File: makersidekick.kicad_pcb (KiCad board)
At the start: 2 copper layers, 58.9 x 22.9 mm, 11 parts, among them J2 Conn_01x12, J4 Conn_01x16

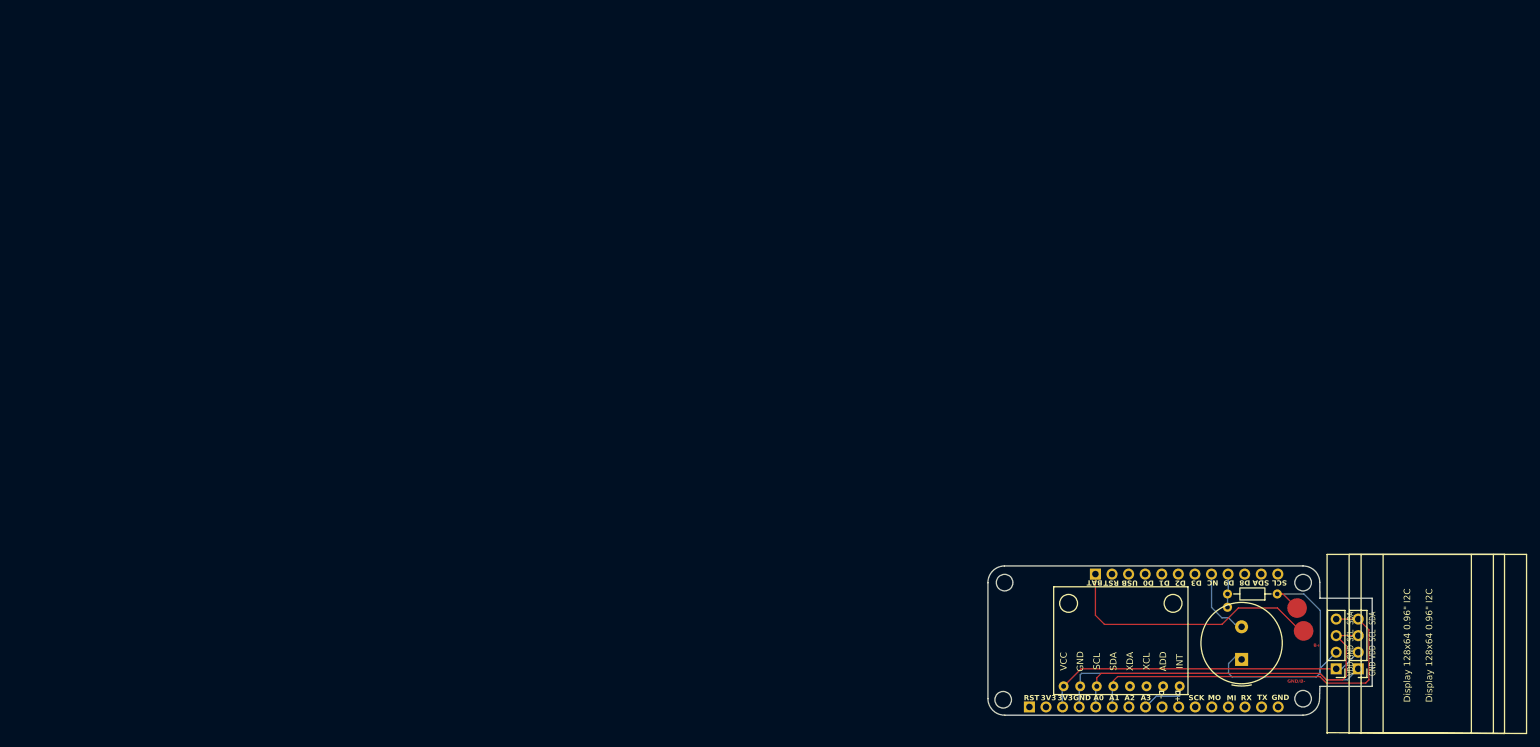
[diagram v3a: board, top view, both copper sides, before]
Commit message: Add buttons, shift text and reroute a lot
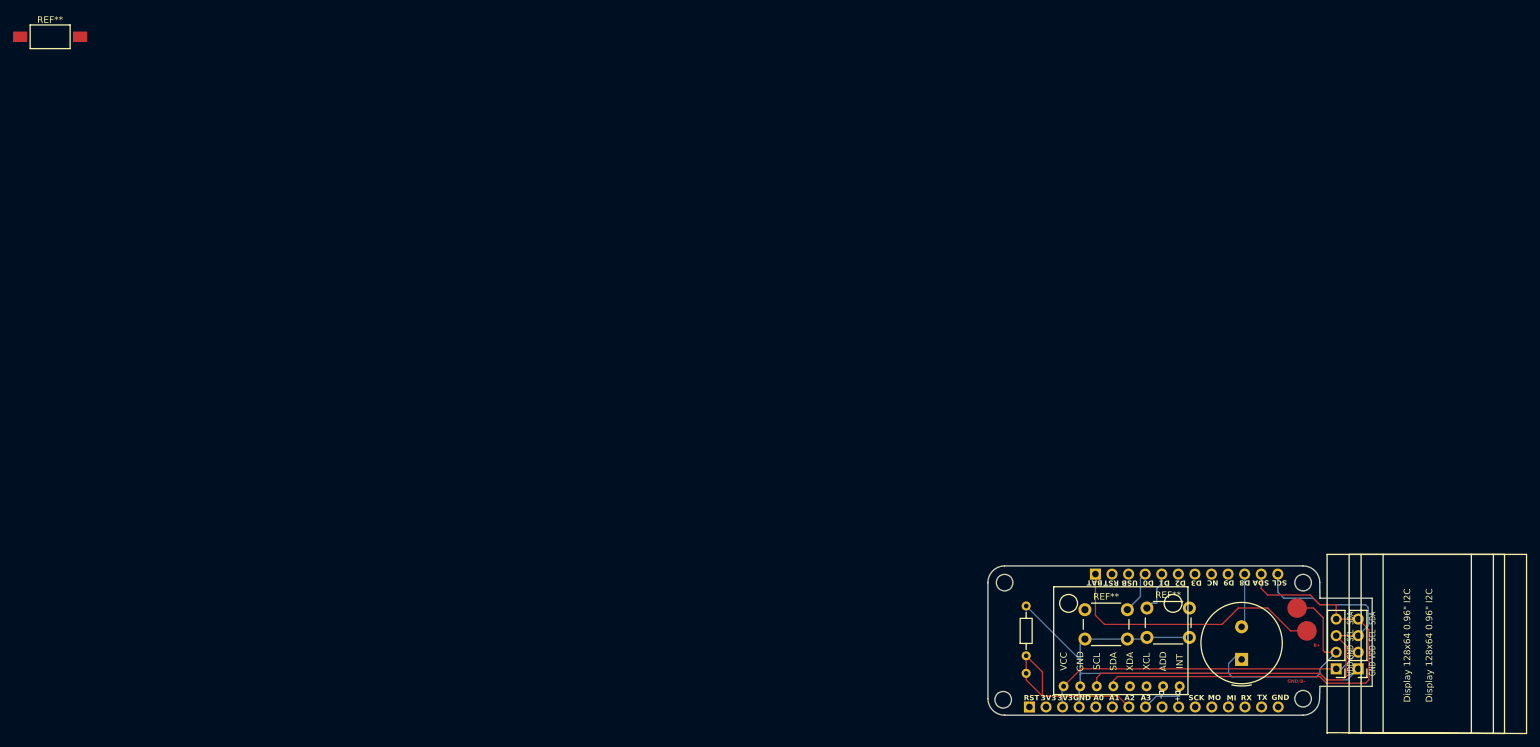
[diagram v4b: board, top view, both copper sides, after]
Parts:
- added REF**: SW_SPST_FSMSM, Button_Switch_SMD:SW_SPST_FSMSM, F.Cu at (0.00, 0.00)
- added REF**: SW_PUSH_6mm_H5mm, Button_Switch_THT:SW_PUSH_6mm_H5mm, F.Cu at (158.5, 87.8)
- added REF**: SW_PUSH_6mm_H5mm, Button_Switch_THT:SW_PUSH_6mm_H5mm, F.Cu at (168.0, 87.5)
- moved REF** 39.6 mm to (149.5, 94.8), turned to 90 degrees
- moved ? 32.5 mm to (149.5, 97.5)
- moved ? 0.50 mm to (192.5, 91.0)
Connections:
- ? pad 2: D9 -> A2
- Display 128x64 0.96" I2C pad 1: (no net) -> gnd
- Display 128x64 0.96" I2C pad 2: (no net) -> 3v3
- Display 128x64 0.96" I2C pad 3: (no net) -> SCL (x2)
- Display 128x64 0.96" I2C pad 4: (no net) -> SDA (x2)
- Display 128x64 0.96" I2C pad 1: (no net) -> 3v3
- Display 128x64 0.96" I2C pad 2: (no net) -> gnd
- J2 pad 10: unconnected-(J2-Pin_10-Pad10) -> D8
- J2 pad 11: unconnected-(J2-Pin_11-Pad11) -> SDA
- J2 pad 12: unconnected-(J2-Pin_12-Pad12) -> SCL
- J2 pad 4: unconnected-(J2-Pin_4-Pad4) -> D0
- J2 pad 5: unconnected-(J2-Pin_5-Pad5) -> D1
- J2 pad 8: D8 -> NC
- J4 pad 7: unconnected-(J4-Pin_7-Pad7) -> A2
- REF** pad 1: gnd -> A2
- REF** pad 2: D9 -> gnd
- REF** pad 3: A0 -> SCL
- REF** pad 4: A1 -> SDA
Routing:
- net SCL: track 0.00 -> 73.4 mm
- net SDA: track 0.00 -> 71.4 mm
- net A1: track 57.5 -> 0.00 mm
- net A0: track 53.9 -> 0.00 mm
- net A2: track 0.00 -> 28.4 mm
- net gnd: track 78.8 -> 101.8 mm
- net D0: track 0.00 -> 6.58 mm
- net D1: track 0.00 -> 6.58 mm
- net D9: track 5.11 -> 0.00 mm
- net D8: track 11.3 -> 8.83 mm
